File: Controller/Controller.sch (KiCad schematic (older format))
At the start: 6 parts

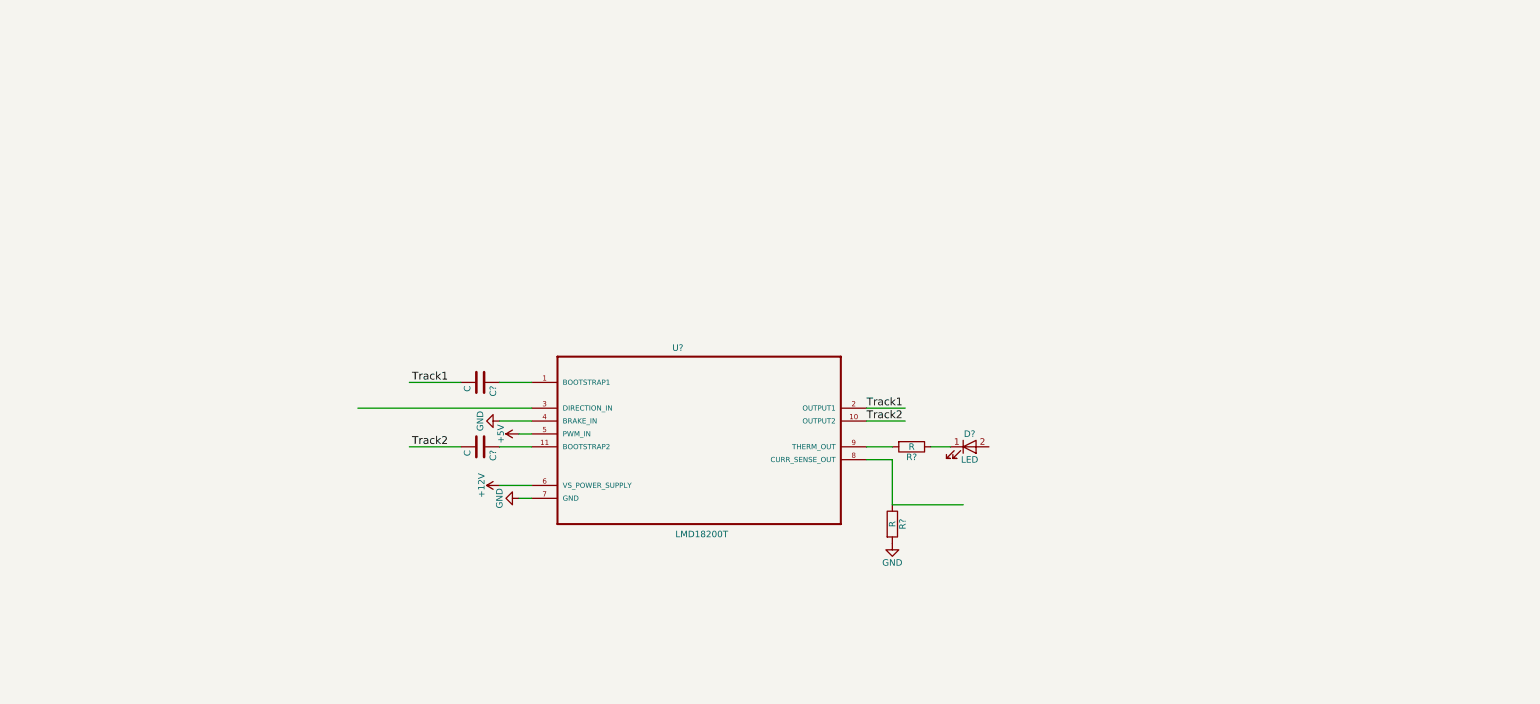
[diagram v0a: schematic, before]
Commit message: Finished schematic. Designed board.
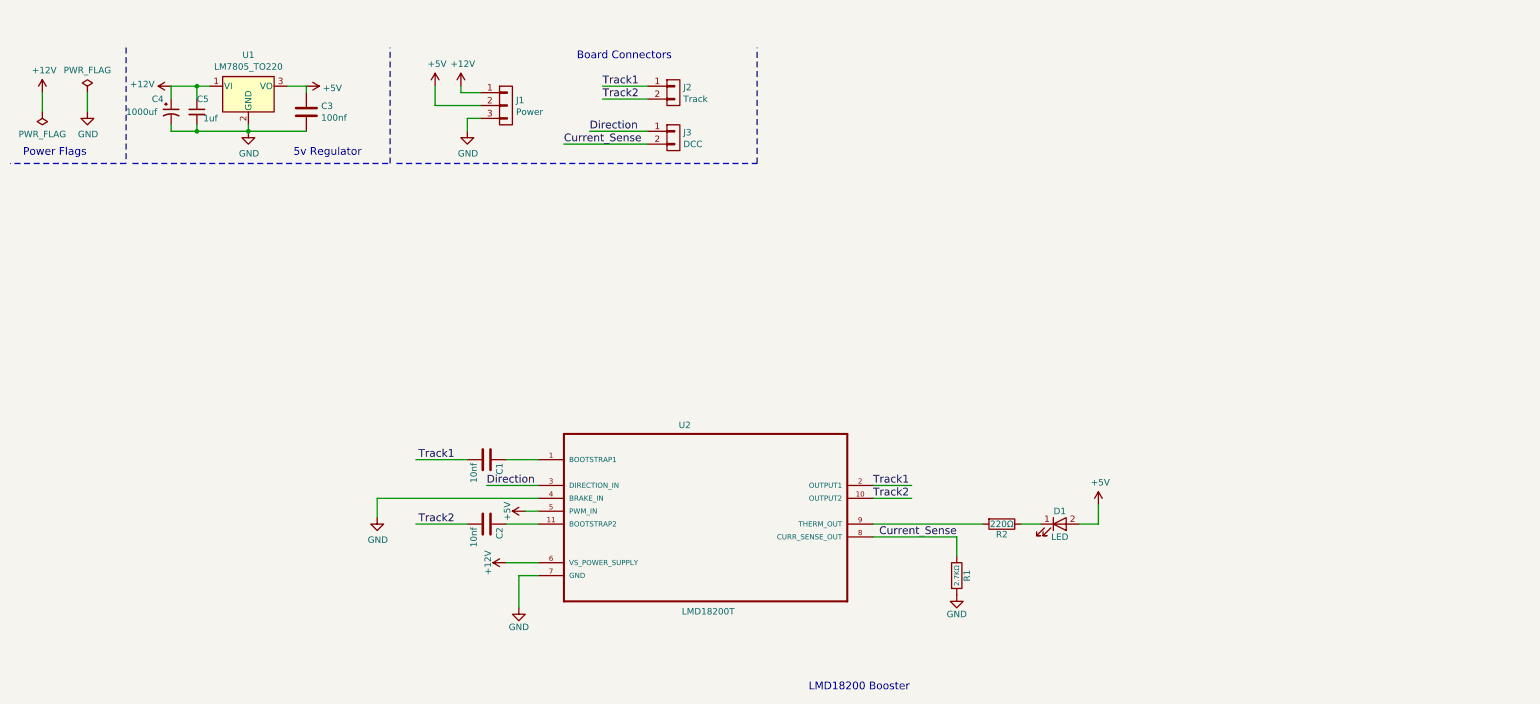
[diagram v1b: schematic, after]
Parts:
- added C3: 100nf, Capacitors_THT:C_Disc_D4.7mm_W2.5mm_P5.00mm, symbol C
- added C4: 1000uf, Capacitors_THT:C_Disc_D4.7mm_W2.5mm_P5.00mm, symbol CP1_Small
- added C5: 1uf, Capacitors_THT:C_Disc_D4.7mm_W2.5mm_P5.00mm, symbol C_Small
- added J1: Power, w_conn_pt-1,5:pt_1,5-3-3,5-h, symbol CONN_01X03
- added J2: Track, w_conn_pt-1,5:pt_1,5-2-3,5-h, symbol CONN_01X02
- added J3: DCC, w_conn_pt-1,5:pt_1,5-2-3,5-h, symbol CONN_01X02
- added U1: LM7805_TO220, TO_SOT_Packages_THT:TO-220-3_Vertical, symbol LM7805_TO220
- C1, C2: renamed from C?; value C -> 10nf; footprint (none) -> Capacitors_THT:C_Disc_D4.7mm_W2.5mm_P5.00mm
- D1: renamed from D?; footprint (none) -> LEDs:LED_0805
- R1: renamed from R?; value R -> 2.7KΩ; footprint (none) -> Resistors_SMD:R_0805
- R2: renamed from R?; value R -> 220Ω; footprint (none) -> Resistors_SMD:R_0805
- U2: renamed from U?; footprint DIOB_LMD18200T -> TO_SOT_Packages_THT:TO-220-11_Vertical_StaggeredType1
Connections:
- net labels added: Current_Sense, Direction
- wire segments 16 -> 40
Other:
- note added: "5v Regulator"
- note added: "Board Connectors"
- note added: "LMD18200 Booster"
- note added: "Power Flags\n"
- moved on the sheet: C1, C2, D1, R1, R2, U2

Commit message: Fixed shortcomings of MINIDCC booster board.
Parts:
- removed J3: DCC, w_conn_pt-1,5:pt_1,5-2-3,5-h, symbol CONN_01X02
- added J3: DCC, Geekboy:pt_1,5-3-3,5-h, symbol conn:Conn_01x03
- C1, C2, C3: symbol C -> device:C
- C4: symbol CP1_Small -> device:CP1_Small
- C5: symbol C_Small -> device:C_Small
- D1: symbol LED -> device:LED
- J1: footprint w_conn_pt-1,5:pt_1,5-3-3,5-h -> Geekboy:pt_1,5-3-3,5-h; symbol CONN_01X03 -> conn:Conn_01x03
- J2: footprint w_conn_pt-1,5:pt_1,5-2-3,5-h -> Geekboy:pt_1,5-2-3,5-h; symbol CONN_01X02 -> conn:Conn_01x02
- R1, R2: symbol R -> device:R
- U1: symbol LM7805_TO220 -> regul:LM7805_TO220
- U2: symbol LMD18200T -> LMD18200T:LMD18200T
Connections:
- wire segments 40 -> 46
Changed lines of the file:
@@
-EESchema Schematic File Version 3
-LIBS:power
-LIBS:device
-LIBS:transistors
-LIBS:conn
-LIBS:linear
-LIBS:regul
-LIBS:74xx
-LIBS:cmos4000
-LIBS:adc-dac
-LIBS:memory
-LIBS:xilinx
-LIBS:microcontrollers
-LIBS:dsp
-LIBS:microchip
-LIBS:analog_switches
-LIBS:motorola
-LIBS:texas
-LIBS:intel
-LIBS:audio
-LIBS:interface
-LIBS:digital-audio
-LIBS:philips
-LIBS:display
-LIBS:cypress
-LIBS:siliconi
-LIBS:opto
-LIBS:atmel
-LIBS:contrib
-LIBS:valves
-LIBS:LMD18200T
+EESchema Schematic File Version 4
 LIBS:Controller-cache
 EELAYER 26 0
@@
 $EndDescr
 $Comp
-L LMD18200T U2
+L LMD18200T:LMD18200T U2
 U 1 1 598F37E3
 P 5900 4000
@@
 $EndComp
 $Comp
-L C C1
+L device:C C1
 U 1 1 598F399B
 P 4200 3700
@@
 $EndComp
 $Comp
-L C C2
+L device:C C2
 U 1 1 598F39E1
 P 4200 4200
@@
 	7200 3900 7500 3900
 $Comp
-L R R2
+L device:R R2
 U 1 1 598F3B8D
 P 8200 4200
@@
 	7200 4200 8050 4200
 $Comp
-L LED D1
+L device:LED D1
 U 1 1 598F3BD0
 P 8650 4200
@@
 	3350 4000 4600 4000
 $Comp
-L +5V #PWR012
+L power:+5V #PWR012
 U 1 1 598FAED1
 P 4500 4100
@@
 	4500 4100 4600 4100
 $Comp
-L GND #PWR011
+L power:GND #PWR011
 U 1 1 598FAFBF
 P 4450 4850
@@
 	4450 4600 4600 4600
 $Comp
-L +12V #PWR010
+L power:+12V #PWR010
 U 1 1 598FAFEF
 P 4350 4500
@@
 	7200 4300 7850 4300
 $Comp
-L R R1
+L device:R R1
 U 1 1 598FCAFD
 P 7850 4600
@@
 $EndComp
 $Comp
-L GND #PWR013
+L power:GND #PWR013
 U 1 1 598FCB20
 P 7850 4750
@@
 $EndComp
 $Comp
-L LM7805_TO220 U1
+L regul:LM7805_TO220 U1
 U 1 1 5A2D8024
 P 2350 800
@@
 $EndComp
 $Comp
-L GND #PWR02
+L power:GND #PWR02
 U 1 1 5A2D8293
 P 1100 1000
@@
 $EndComp
 $Comp
-L +12V #PWR01
+L power:+12V #PWR01
 U 1 1 5A2D8302
 P 750 850
@@
 $EndComp
 $Comp
-L +5V #PWR05
+L power:+5V #PWR05
 U 1 1 5A2D86C1
 P 2800 800
@@
 	2800 800  2650 800
 $Comp
-L GND #PWR04
+L power:GND #PWR04
 U 1 1 5A2D872D
 P 2350 1150
@@
 $EndComp
 $Comp
-L +12V #PWR03
+L power:+12V #PWR03
 U 1 1 5A2D87AB
 P 1750 800
@@
 $EndComp
 Wire Wire Line
-	1750 800  2050 800
-$Comp
-L +5V #PWR014
+	1750 800  1950 800
+$Comp
+L power:+5V #PWR014
 U 1 1 5A2D88F2
 P 8950 4050
@@
 	8950 4200 8800 4200
 $Comp
-L PWR_FLAG #FLG02
+L power:PWR_FLAG #FLG02
 U 1 1 5A2D8DEB
 P 1100 850
@@
 	1100 850  1100 1000
 $Comp
-L PWR_FLAG #FLG01
+L power:PWR_FLAG #FLG01
 U 1 1 5A2D8E62
 P 750 1000
@@
 	8950 4050 8950 4200
 $Comp
-L GND #PWR06
+L power:GND #PWR06
 U 1 1 5A2D91B2
 P 3350 4150
@@
 	7850 4300 7850 4450
 $Comp
-L CONN_01X02 J3
-U 1 1 5A2D9689
-P 5650 1200
-F 0 "J3" H 5727 1241 50  0000 L CNN
-F 1 "DCC" H 5727 1150 50  0000 L CNN
-F 2 "w_conn_pt-1,5:pt_1,5-2-3,5-h" H 5650 1200 50  0001 C CNN
-F 3 "" H 5650 1200 50  0001 C CNN
-	1    5650 1200
-	1    0    0    -1
-$EndComp
-$Comp
-L CONN_01X02 J2
+L conn:Conn_01x02 J2
 U 1 1 5A2D970D
-P 5650 850
-F 0 "J2" H 5727 891 50  0000 L CNN
-F 1 "Track" H 5727 800 50  0000 L CNN
-F 2 "w_conn_pt-1,5:pt_1,5-2-3,5-h" H 5650 850 50  0001 C CNN
-F 3 "" H 5650 850 50  0001 C CNN
-	1    5650 850
-	1    0    0    -1
-$EndComp
-$Comp
-L CONN_01X03 J1
+P 5950 800
+F 0 "J2" H 6027 841 50  0000 L CNN
+F 1 "Track" H 6027 750 50  0000 L CNN
+F 2 "Geekboy:pt_1,5-2-3,5-h" H 5950 800 50  0001 C CNN
+F 3 "" H 5950 800 50  0001 C CNN
+	1    5950 800
+	1    0    0    -1
+$EndComp
+$Comp
+L conn:Conn_01x03 J1
 U 1 1 5A2D97C5
 P 4350 950
 F 0 "J1" H 4428 991 50  0000 L CNN
 F 1 "Power" H 4428 900 50  0000 L CNN
-F 2 "w_conn_pt-1,5:pt_1,5-3-3,5-h" H 4350 950 50  0001 C CNN
+F 2 "Geekboy:pt_1,5-3-3,5-h" H 4350 950 50  0001 C CNN
 F 3 "" H 4350 950 50  0001 C CNN
 	1    4350 950
 	1    0    0    -1
 $EndComp
-Text Label 5100 800  0    60   ~ 0
+Text Label 5400 800  0    60   ~ 0
 Track1
 Wire Wire Line
-	5450 800  5100 800
-Text Label 5100 900  0    60   ~ 0
+	5750 800  5400 800
+Text Label 5400 900  0    60   ~ 0
 Track2
 Wire Wire Line
-	5100 900  5450 900
-Text Label 5000 1150 0    60   ~ 0
+	5400 900  5750 900
+Text Label 4850 1000 0    60   ~ 0
 Direction
 Wire Wire Line
-	5000 1150 5450 1150
-Text Label 4800 1250 0    60   ~ 0
+	4850 1000 5300 1000
+Text Label 4650 1100 0    60   ~ 0
 Current_Sense
 Wire Wire Line
-	4800 1250 5450 1250
-$Comp
-L +12V #PWR08
+	4650 1100 5300 1100
+$Comp
+L power:+12V #PWR08
 U 1 1 5A2DA022
 P 4000 800
@@
 	4000 850  4150 850
 $Comp
-L +5V #PWR07
+L power:+5V #PWR07
 U 1 1 5A2DA0B7
 P 3800 800
@@
 	3800 950  4150 950
 $Comp
-L GND #PWR09
+L power:GND #PWR09
 U 1 1 5A2DA14F
 P 4050 1150
@@
 LMD18200 Booster
 $Comp
-L C C3
+L device:C C3
 U 1 1 5A2DBB14
 P 2800 1000
@@
 $EndComp
 Wire Wire Line
-	1750 1150 2800 1150
+	1750 1150 1950 1150
 Wire Wire Line
 	2800 800  2800 850
 $Comp
-L CP1_Small C4
+L device:CP1_Small C4
 U 1 1 5A2DC31F
 P 1750 1000
@@
 Connection ~ 1950 1150
 $Comp
-L C_Small C5
+L device:C_Small C5
 U 1 1 5A2DC812
 P 1950 1000
@@
 	1    0    0    -1
 $EndComp
+Wire Wire Line
+	2350 1150 2800 1150
+Wire Wire Line
+	1950 800  2050 800
+Wire Wire Line
+	1950 1150 2350 1150
+$Comp
+L conn:Conn_01x03 J3
+U 1 1 5A9E104B
+P 5500 1100
+F 0 "J3" H 5578 1141 50  0000 L CNN
+F 1 "DCC" H 5578 1050 50  0000 L CNN
+F 2 "Geekboy:pt_1,5-3-3,5-h" H 5500 1100 50  0001 C CNN
+F 3 "" H 5500 1100 50  0001 C CNN
+	1    5500 1100
+	1    0    0    -1
+$EndComp
+$Comp
+L power:GND #PWR015
+U 1 1 5A9E2602
+P 5150 1200
+F 0 "#PWR015" H 5150 950 50  0001 C CNN
+F 1 "GND" H 5155 1027 50  0000 C CNN
+F 2 "" H 5150 1200 50  0001 C CNN
+F 3 "" H 5150 1200 50  0001 C CNN
+	1    5150 1200
+	1    0    0    -1
+$EndComp
+Wire Wire Line
+	6050 3450 12300 3450
+Wire Wire Line
+	12300 3450 12300 2700
+Wire Wire Line
+	5150 1200 5300 1200
 $EndSCHEMATC

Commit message: Added silk screen text. Fixed fubars from last commit.
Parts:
- C4: footprint Capacitors_THT:C_Disc_D4.7mm_W2.5mm_P5.00mm -> Capacitors_THT:CP_Radial_D10.0mm_P5.00mm
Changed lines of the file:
@@
 F 0 "C4" H 1600 1100 50  0000 L CNN
 F 1 "1000uf" H 1400 1000 50  0000 L CNN
-F 2 "Capacitors_THT:C_Disc_D4.7mm_W2.5mm_P5.00mm" H 1750 1000 50  0001 C CNN
+F 2 "Capacitors_THT:CP_Radial_D10.0mm_P5.00mm" H 1750 1000 50  0001 C CNN
 F 3 "" H 1750 1000 50  0001 C CNN
 	1    1750 1000
